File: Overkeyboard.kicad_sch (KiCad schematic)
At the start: 340 parts, among them SW1 SW_Push, SW10 SW_Push, SW100 SW_Push, SW101 SW_Push, SW102 SW_Push, SW103 SW_Push, SW104 SW_Push, SW105 SW_Push, SW106 SW_Push, SW107 SW_Push, SW108 SW_Push, SW109 SW_Push, SW11 SW_Push, SW110 SW_Push, SW111 SW_Push, SW112 SW_Push, SW113 SW_Push, SW114 SW_Push, SW115 SW_Push, SW116 SW_Push, SW117 SW_Push, SW118 SW_Push, SW119 SW_Push, SW12 SW_Push, SW120 SW_Push, SW121 SW_Push, SW122 SW_Push, SW123 SW_Push, SW124 SW_Push, SW125 SW_Push, SW126 SW_Push, SW127 SW_Push, SW128 SW_Push, SW129 SW_Push, SW13 SW_Push, SW130 SW_Push, SW131 SW_Push, SW132 SW_Push, SW133 SW_Push, SW134 SW_Push, SW135 SW_Push, SW136 SW_Push, SW137 SW_Push, SW138 SW_Push, SW139 SW_Push, SW14 SW_Push, SW140 SW_Push, SW141 SW_Push, SW142 SW_Push, SW143 SW_Push, SW144 SW_Push, SW145 SW_Push, SW146 SW_Push, SW147 SW_Push, SW148 SW_Push, SW149 SW_Push, SW15 SW_Push, SW150 SW_Push, SW151 SW_Push, SW152 SW_Push, SW153 SW_Push, SW154 SW_Push, SW155 SW_Push, SW156 SW_Push, SW157 SW_Push, SW158 SW_Push, SW16 SW_Push, SW17 SW_Push, SW18 SW_Push, SW19 SW_Push, SW2 SW_Push, SW20 SW_Push, SW21 SW_Push, SW22 SW_Push, SW23 SW_Push, SW24 SW_Push, SW25 SW_Push, SW26 SW_Push, SW27 SW_Push, SW28 SW_Push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

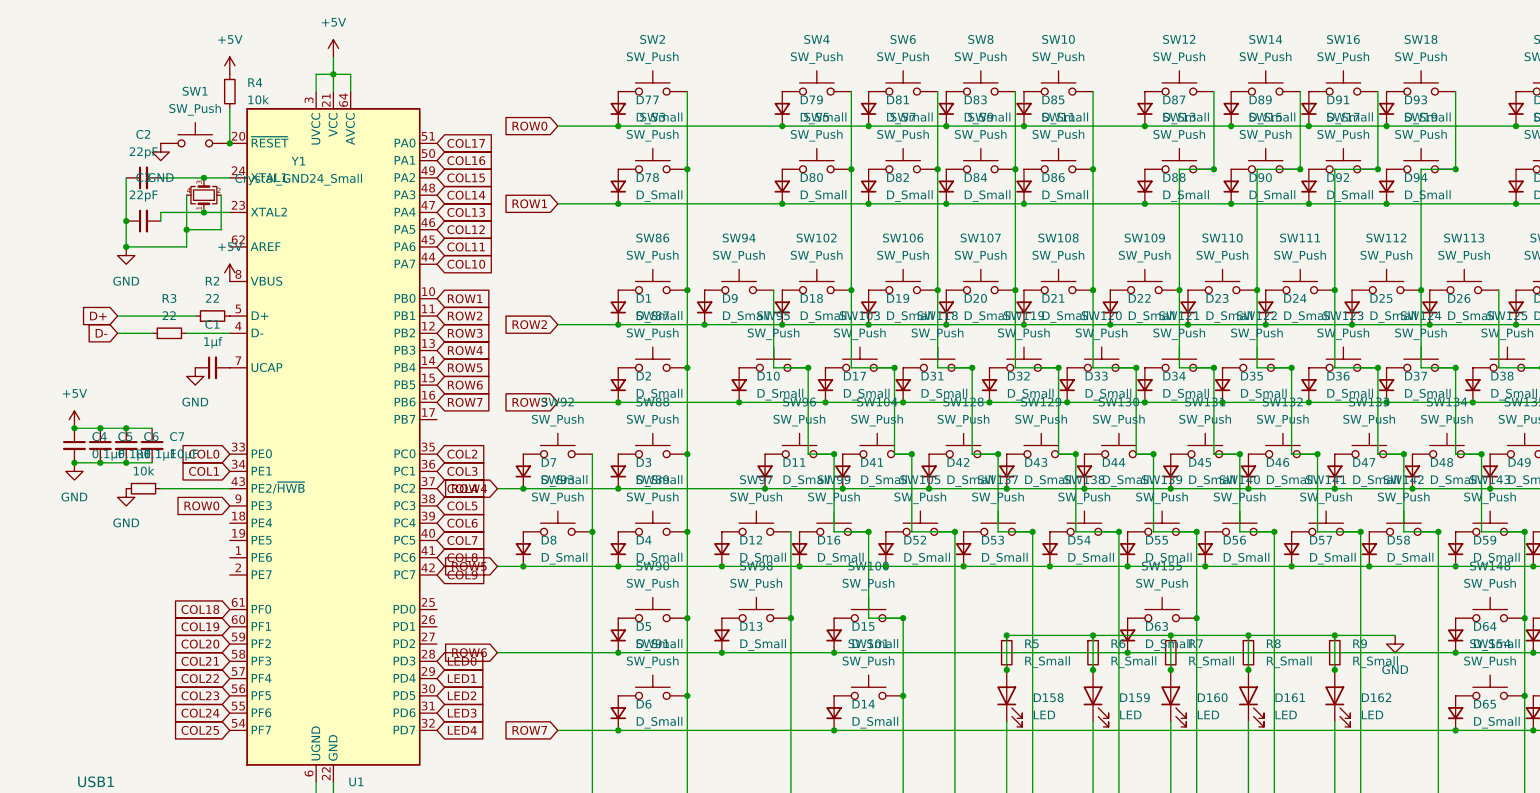
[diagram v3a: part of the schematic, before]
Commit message: slight wiring changes and LED resistor values determined
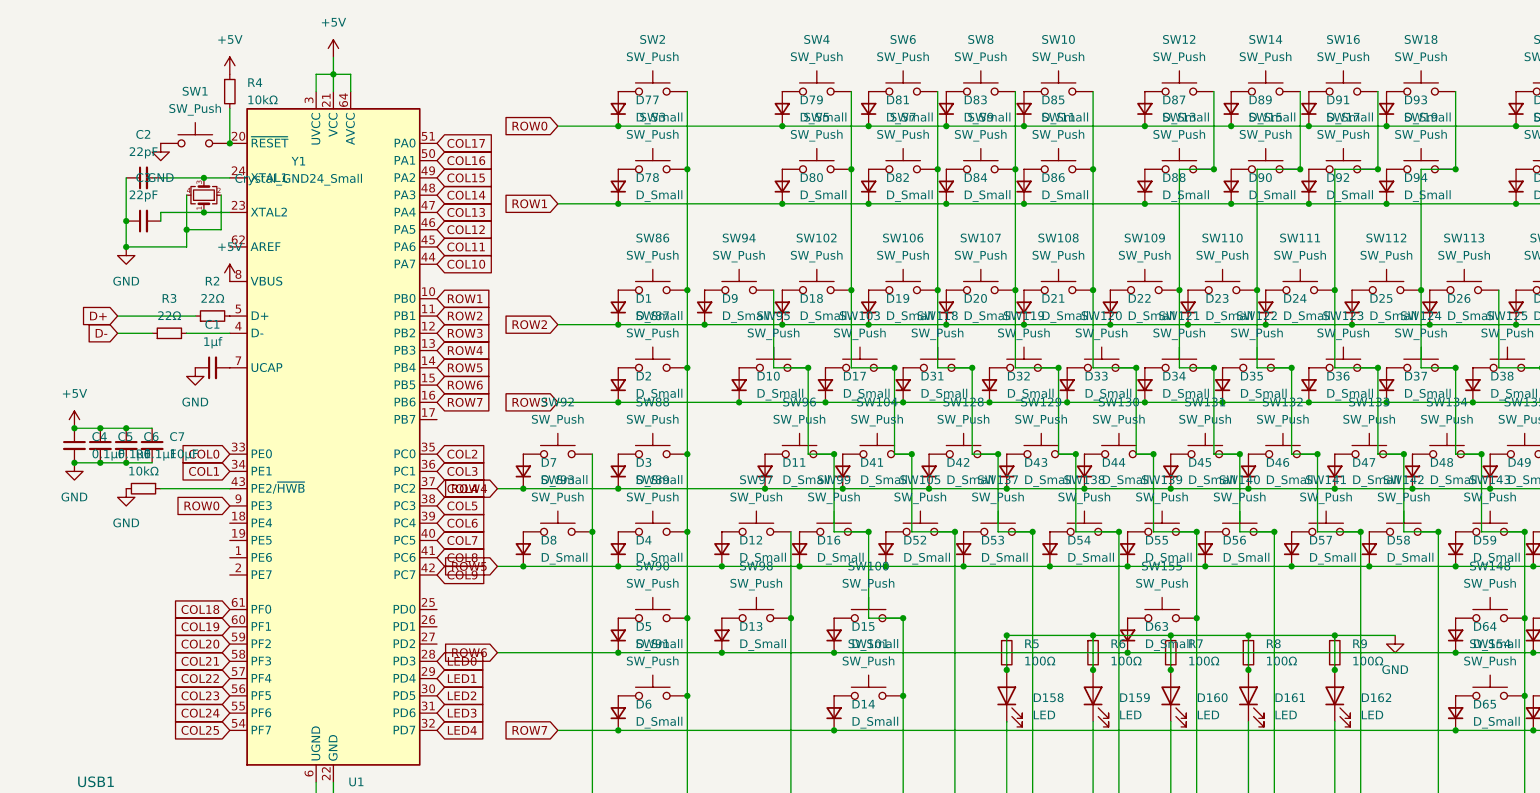
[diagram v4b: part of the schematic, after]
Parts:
- R1, R4: value 10k -> 10kΩ
- R2, R3: value 22 -> 22Ω
- R5, R6, R7, R8, R9: value R_Small -> 100Ω
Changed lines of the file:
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@@
 			)
 		)
-		(property "Value" "22"
+		(property "Value" "22Ω"
 			(at 27.94 53.34 90)
 			(effects
@@
 			)
 		)
-		(property "Value" "R_Small"
+		(property "Value" "100Ω"
 			(at 153.67 104.1399 0)
 			(effects
@@
 			)
 		)
-		(property "Value" "R_Small"
+		(property "Value" "100Ω"
 			(at 177.8 104.1399 0)
 			(effects
@@
 			)
 		)
-		(property "Value" "22"
+		(property "Value" "22Ω"
 			(at 34.29 50.8 90)
 			(effects
@@
 			)
 		)
-		(property "Value" "10k"
+		(property "Value" "10kΩ"
 			(at 24.13 76.2 90)
 			(effects
@@
 			)
 		)
-		(property "Value" "R_Small"
+		(property "Value" "100Ω"
 			(at 189.23 104.1399 0)
 			(effects
@@
 			)
 		)
-		(property "Value" "R_Small"
+		(property "Value" "100Ω"
 			(at 166.37 104.1399 0)
 			(effects
@@
 			)
 		)
-		(property "Value" "10k"
+		(property "Value" "10kΩ"
 			(at 39.37 21.5899 0)
 			(effects
@@
 			)
 		)
-		(property "Value" "R_Small"
+		(property "Value" "100Ω"
 			(at 201.93 104.1399 0)
 			(effects
